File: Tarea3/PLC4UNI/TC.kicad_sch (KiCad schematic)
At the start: 0 parts

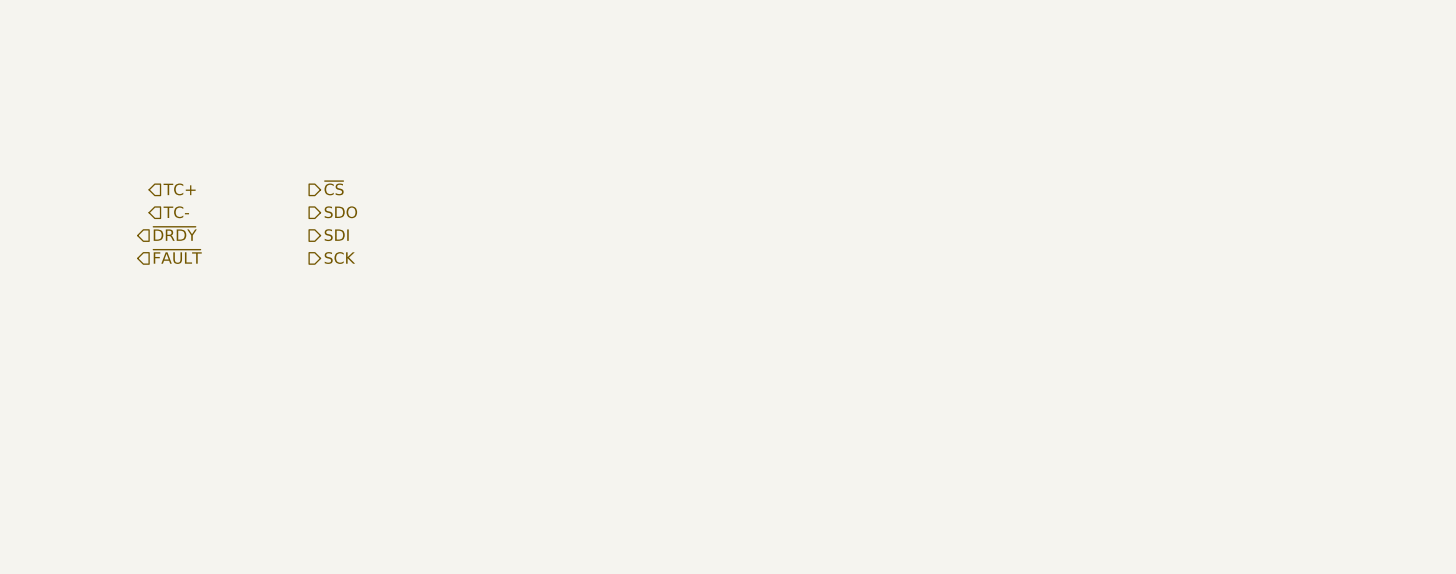
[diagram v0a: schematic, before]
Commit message: Cambio de directorio [Tarea2->CAD]
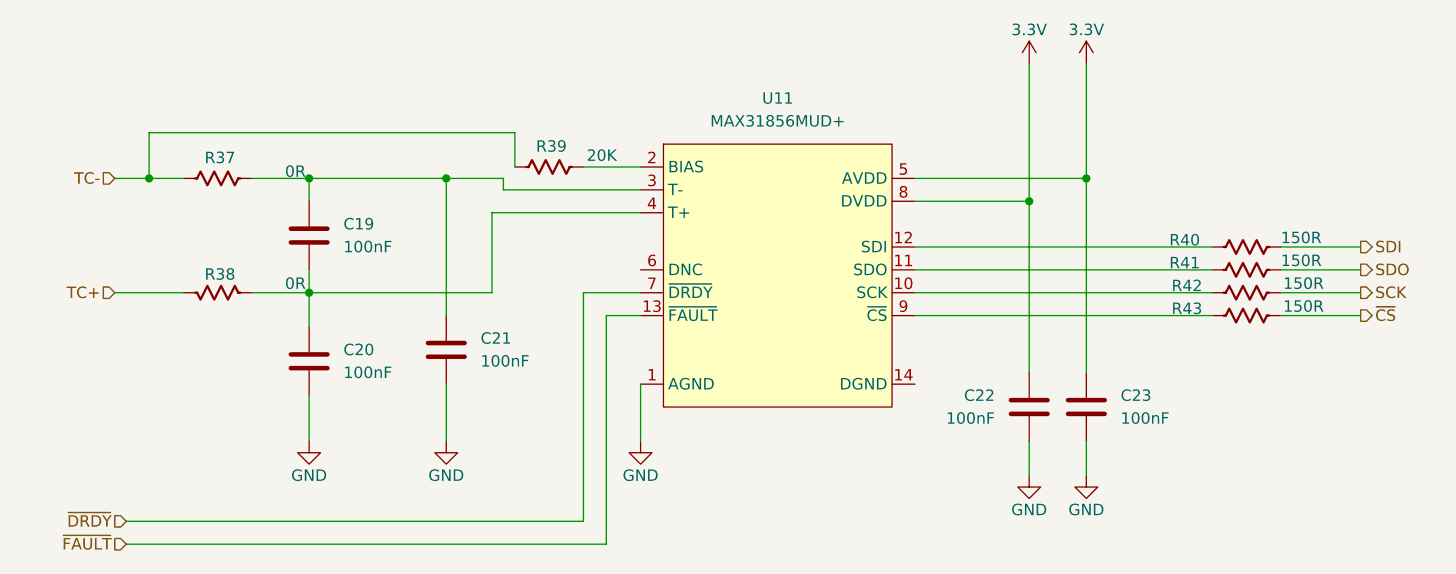
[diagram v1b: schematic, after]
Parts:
- added C19, C20, C21, C22, C23: 100nF, PCM_Capacitor_SMD_AKL:C_0603_1608Metric, symbol PCM_Capacitor_US_AKL:C_0603
- added R37, R38: 0R, PCM_Resistor_SMD_AKL:R_0603_1608Metric, symbol PCM_Resistor_US_AKL:R_0603
- added R39: 20K, PCM_Resistor_SMD_AKL:R_0603_1608Metric, symbol PCM_Resistor_US_AKL:R_0603
- added R40, R41, R42, R43: 150R, PCM_Resistor_SMD_AKL:R_0603_1608Metric, symbol PCM_Resistor_US_AKL:R_0603
- added U11: MAX31856MUD+, EasyEDA:TSSOP-14_L5.0-W4.4-P0.65-LS6.4-BL, symbol EasyEDA:MAX31856MUD+
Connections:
- net SCK: now also R42.2
- net SDI: now also R40.2
- net SDO: now also R41.2
- net TC+: now also R38.2
- net TC-: now also R37.1, R39.1
- net ~{CS}: now also R43.2
- net ~{DRDY}: now also U11.7 (~{DRDY})
- net ~{FAULT}: now also U11.13 (~{FAULT})
- new net: C19.1, C21.1, R37.2, U11.3 (T-)
- new net: C19.2, C20.1, R38.1, U11.4 (T+)
- new net: R41.1, U11.11 (SDO)
- new net: R40.1, U11.12 (SDI)
- new net: R43.1, U11.9 (~{CS})
- new net: R39.2, U11.2 (BIAS)
- new net: R42.1, U11.10 (SCK)
- new net 3.3V: C22.1, C23.1, U11.5 (AVDD), U11.8 (DVDD)
- new net GND: C20.2, C21.2, C22.2, C23.2, U11.1 (AGND)
